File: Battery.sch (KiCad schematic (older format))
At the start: 23 parts, among them J3 USB_C_Receptacle_USB2.0, SW2 SW_SPDT, U4 SY6926

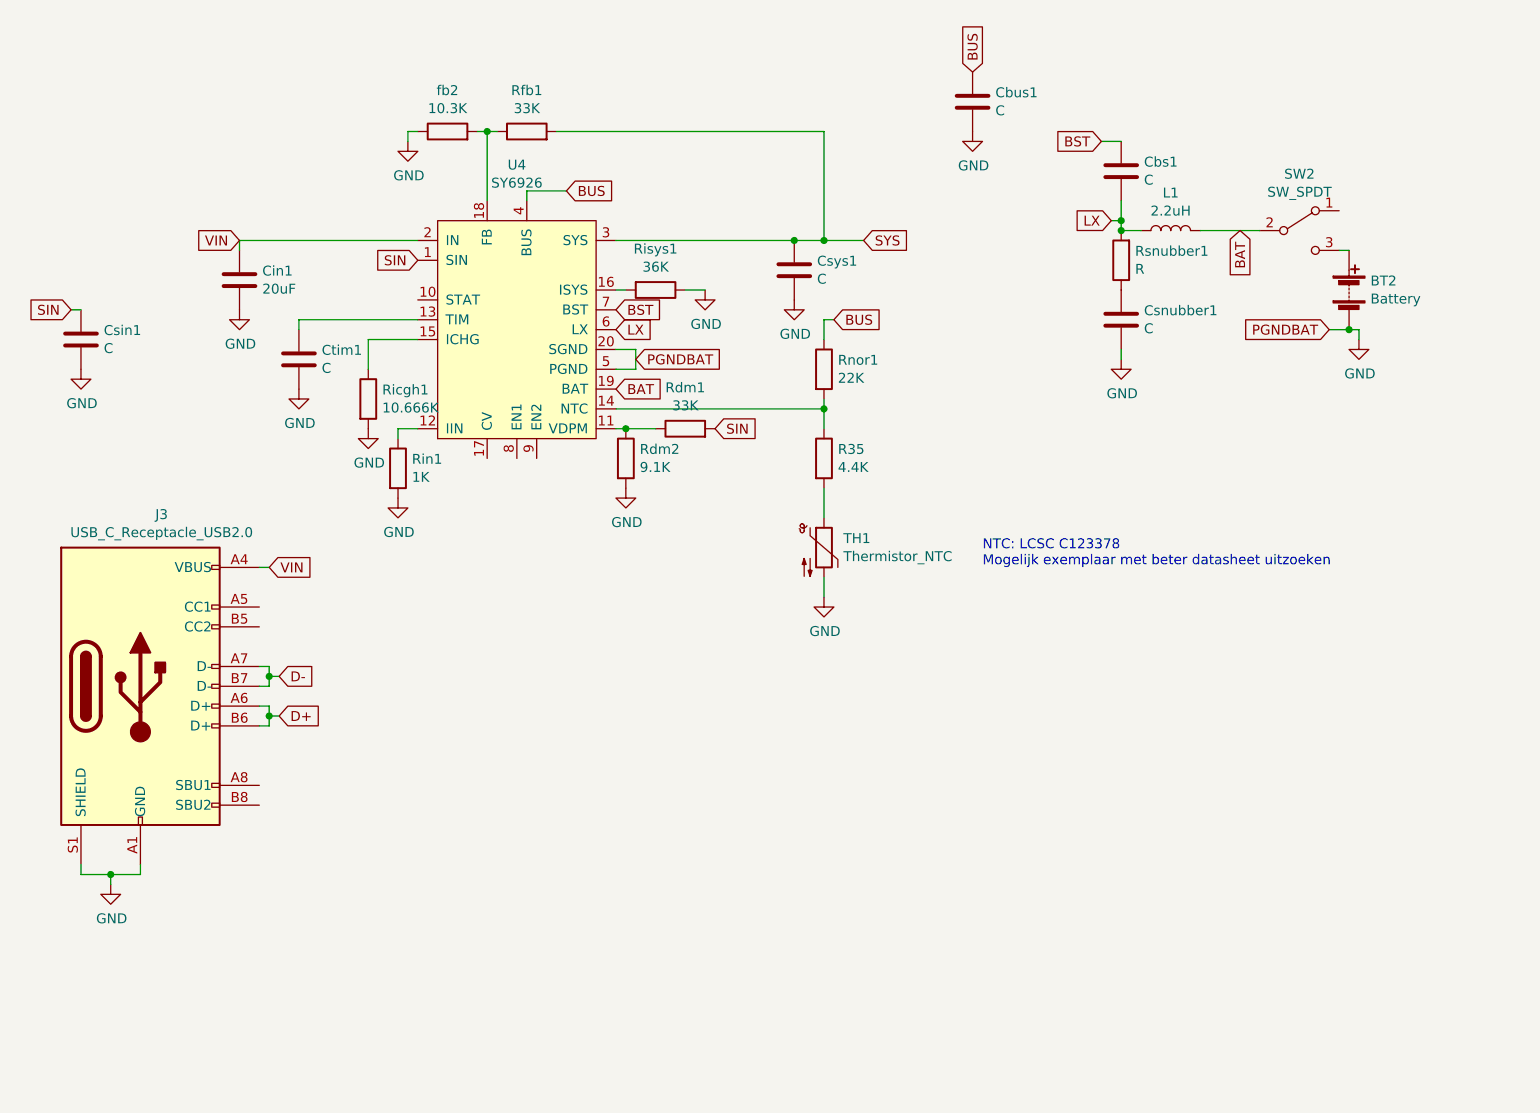
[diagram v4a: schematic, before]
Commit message: Added a rotary encoder and almost all BC values
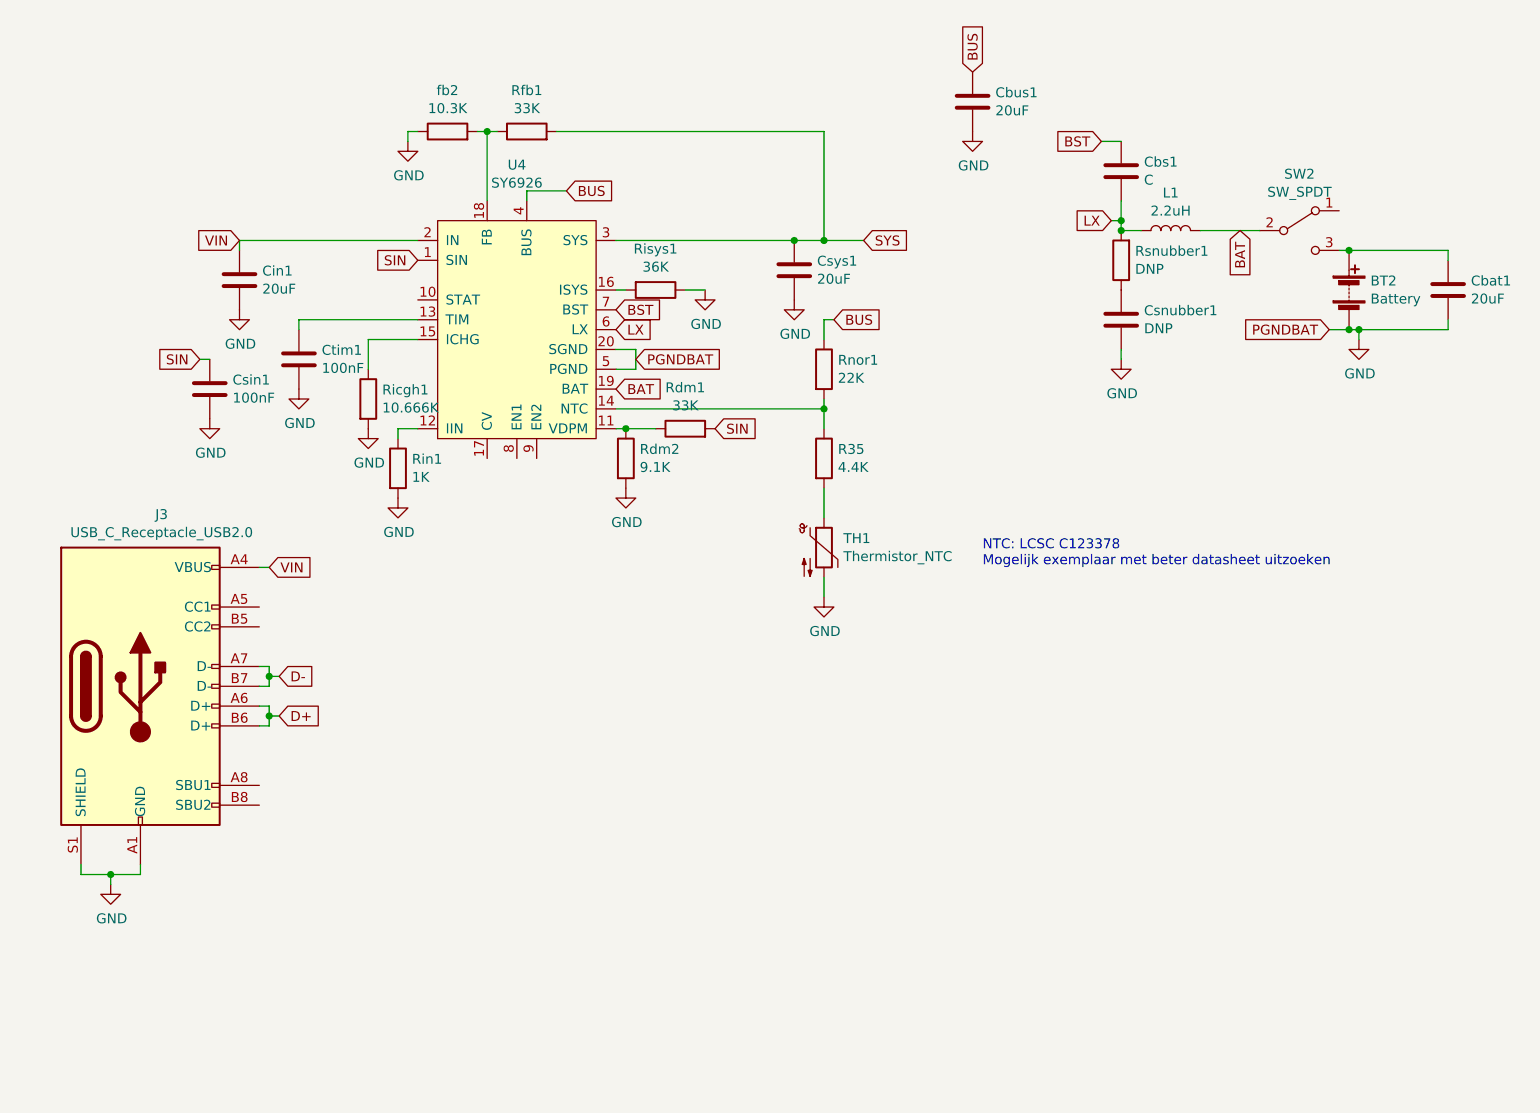
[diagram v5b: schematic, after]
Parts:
- added Cbat1: 20uF, Capacitor_SMD:C_0805_2012Metric, symbol Device:C
- Cbus1, Csys1: value C -> 20uF
- Csin1, Ctim1: value C -> 100nF
- Csnubber1: value C -> DNP
- Rsnubber1: value R -> DNP
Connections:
- net GND: now also Cbat1.2
- net at BT2.1 (+), SW2.3 (C): now also Cbat1.1
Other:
- moved on the sheet: Csin1
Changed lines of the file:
@@
-$EndComp
-$Comp
-L Device:C Cbs1
-U 1 1 60BFBF81
-P 6150 1800
-F 0 "Cbs1" H 6265 1846 50  0000 L CNN
-F 1 "C" H 6265 1755 50  0000 L CNN
-F 2 "Capacitor_SMD:C_0805_2012Metric" H 6188 1650 50  0001 C CNN
-F 3 "~" H 6150 1800 50  0001 C CNN
-	1    6150 1800
-	1    0    0    -1
 $EndComp
 $Comp
@@
 P 2000 2750
 F 0 "Ctim1" H 2115 2796 50  0000 L CNN
-F 1 "C" H 2115 2705 50  0000 L CNN
+F 1 "100nF" H 2115 2705 50  0000 L CNN
 F 2 "Capacitor_SMD:C_0805_2012Metric" H 2038 2600 50  0001 C CNN
 F 3 "~" H 2000 2750 50  0001 C CNN
@@
 L Device:C Csin1
 U 1 1 60C0200C
-P 900 2650
-F 0 "Csin1" H 1015 2696 50  0000 L CNN
-F 1 "C" H 1015 2605 50  0000 L CNN
-F 2 "Capacitor_SMD:C_0805_2012Metric" H 938 2500 50  0001 C CNN
-F 3 "~" H 900 2650 50  0001 C CNN
-	1    900  2650
+P 1550 2900
+F 0 "Csin1" H 1665 2946 50  0000 L CNN
+F 1 "100nF" H 1665 2855 50  0000 L CNN
+F 2 "Capacitor_SMD:C_0805_2012Metric" H 1588 2750 50  0001 C CNN
+F 3 "~" H 1550 2900 50  0001 C CNN
+	1    1550 2900
 	1    0    0    -1
 $EndComp
@@
 P 4500 2300
 F 0 "Csys1" H 4615 2346 50  0000 L CNN
-F 1 "C" H 4615 2255 50  0000 L CNN
+F 1 "20uF" H 4615 2255 50  0000 L CNN
 F 2 "Capacitor_SMD:C_0805_2012Metric" H 4538 2150 50  0001 C CNN
 F 3 "~" H 4500 2300 50  0001 C CNN
@@
 	6050 1650 6150 1650
 $Comp
-L Device:R Rsnubber1
-U 1 1 60C19527
-P 6150 2250
-F 0 "Rsnubber1" H 6080 2204 50  0000 R CNN
-F 1 "R" H 6080 2295 50  0000 R CNN
-F 2 "Resistor_SMD:R_0805_2012Metric" V 6080 2250 50  0001 C CNN
-F 3 "~" H 6150 2250 50  0001 C CNN
-	1    6150 2250
-	-1   0    0    1
-$EndComp
-$Comp
 L Device:C Csnubber1
 U 1 1 60C1A249
 P 6150 2550
 F 0 "Csnubber1" H 6265 2596 50  0000 L CNN
-F 1 "C" H 6265 2505 50  0000 L CNN
+F 1 "DNP" H 6265 2505 50  0000 L CNN
 F 2 "Capacitor_SMD:C_0805_2012Metric" H 6188 2400 50  0001 C CNN
 F 3 "~" H 6150 2550 50  0001 C CNN
@@
 L power:GND #PWR01
 U 1 1 60C26847
-P 900 2800
-F 0 "#PWR01" H 900 2550 50  0001 C CNN
-F 1 "GND" H 905 2627 50  0000 C CNN
-F 2 "" H 900 2800 50  0001 C CNN
-F 3 "" H 900 2800 50  0001 C CNN
-	1    900  2800
+P 1550 3050
+F 0 "#PWR01" H 1550 2800 50  0001 C CNN
+F 1 "GND" H 1555 2877 50  0000 C CNN
+F 2 "" H 1550 3050 50  0001 C CNN
+F 3 "" H 1550 3050 50  0001 C CNN
+	1    1550 3050
 	1    0    0    -1
 $EndComp
@@
 Wire Wire Line
 	2000 2550 2000 2600
-Text GLabel 850  2500 0    50   Input ~ 0
+Text GLabel 1500 2750 0    50   Input ~ 0
 SIN
 Wire Wire Line
-	850  2500 900  2500
+	1500 2750 1550 2750
 $Comp
 L Device:R fb2
@@
 P 5400 1450
 F 0 "Cbus1" H 5515 1496 50  0000 L CNN
-F 1 "C" H 5515 1405 50  0000 L CNN
+F 1 "20uF" H 5515 1405 50  0000 L CNN
 F 2 "Capacitor_SMD:C_0805_2012Metric" H 5438 1300 50  0001 C CNN
 F 3 "~" H 5400 1450 50  0001 C CNN
@@
 Wire Wire Line
 	3600 3000 4650 3000
+$Comp
+L Device:R Rsnubber1
+U 1 1 60C19527
+P 6150 2250
+F 0 "Rsnubber1" H 6080 2204 50  0000 R CNN
+F 1 "DNP" H 6080 2295 50  0000 R CNN
+F 2 "Resistor_SMD:R_0805_2012Metric" V 6080 2250 50  0001 C CNN
+F 3 "~" H 6150 2250 50  0001 C CNN
+	1    6150 2250
+	-1   0    0    1
+$EndComp
+$Comp
+L Device:C Cbs1
+U 1 1 60BFBF81
+P 6150 1800
+F 0 "Cbs1" H 6265 1846 50  0000 L CNN
+F 1 "C" H 6265 1755 50  0000 L CNN
+F 2 "Capacitor_SMD:C_0805_2012Metric" H 6188 1650 50  0001 C CNN
+F 3 "~" H 6150 1800 50  0001 C CNN
+	1    6150 1800
+	1    0    0    -1
+$EndComp
+$Comp
+L Device:C Cbat1
+U 1 1 60D9E5BD
+P 7800 2400
+F 0 "Cbat1" H 7915 2446 50  0000 L CNN
+F 1 "20uF" H 7915 2355 50  0000 L CNN
+F 2 "Capacitor_SMD:C_0805_2012Metric" H 7838 2250 50  0001 C CNN
+F 3 "~" H 7800 2400 50  0001 C CNN
+	1    7800 2400
+	1    0    0    -1
+$EndComp
+Wire Wire Line
+	7300 2200 7800 2200
+Wire Wire Line
+	7800 2200 7800 2250
+Connection ~ 7300 2200
+Wire Wire Line
+	7800 2550 7800 2600
+Wire Wire Line
+	7800 2600 7350 2600
+Connection ~ 7350 2600
 $EndSCHEMATC

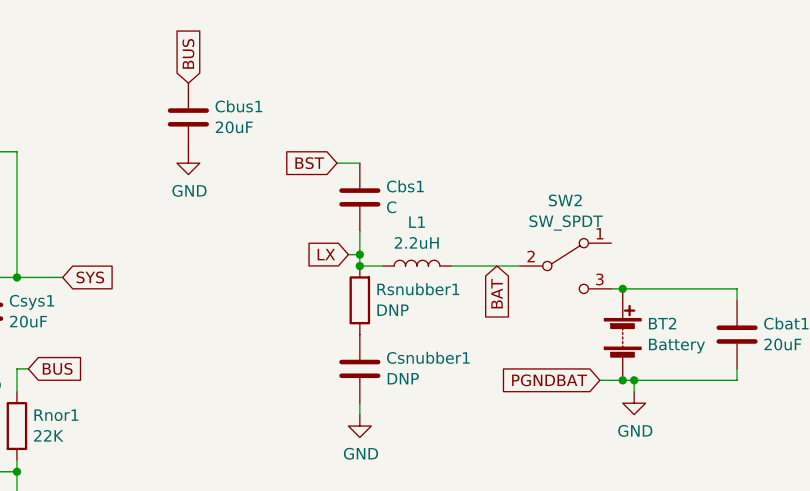
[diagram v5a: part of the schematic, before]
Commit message: Final schematic edits, PCB layout
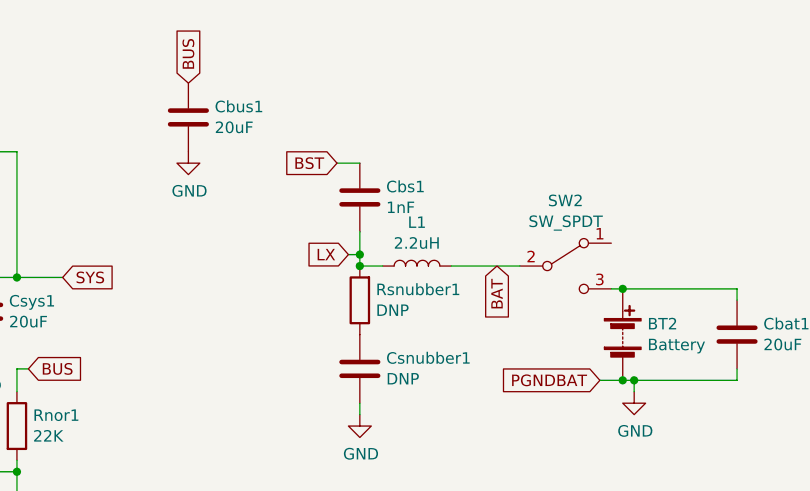
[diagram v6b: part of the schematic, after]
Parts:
- Cbs1: value C -> 1nF
- L1: footprint Connector_PinHeader_2.54mm:PinHeader_1x02_P2.54mm_Vertical -> Inductor_SMD:L_Sunlord_MWSA0518_5.4x5.2mm
- R35: footprint (none) -> Resistor_SMD:R_0805_2012Metric
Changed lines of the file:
@@
 $Descr A4 11693 8268
 encoding utf-8
-Sheet 3 5
+Sheet 3 6
 Title "Battery"
 Date ""
@@
 F 0 "L1" V 6590 2100 50  0000 C CNN
 F 1 "2.2uH" V 6499 2100 50  0000 C CNN
-F 2 "Connector_PinHeader_2.54mm:PinHeader_1x02_P2.54mm_Vertical" H 6400 2100 50  0001 C CNN
+F 2 "Inductor_SMD:L_Sunlord_MWSA0518_5.4x5.2mm" H 6400 2100 50  0001 C CNN
 F 3 "~" H 6400 2100 50  0001 C CNN
 	1    6400 2100
@@
 F 0 "R35" H 4720 3296 50  0000 L CNN
 F 1 "4.4K" H 4720 3205 50  0000 L CNN
-F 2 "" V 4580 3250 50  0001 C CNN
+F 2 "Resistor_SMD:R_0805_2012Metric" V 4580 3250 50  0001 C CNN
 F 3 "~" H 4650 3250 50  0001 C CNN
 	1    4650 3250
@@
 P 6150 1800
 F 0 "Cbs1" H 6265 1846 50  0000 L CNN
-F 1 "C" H 6265 1755 50  0000 L CNN
+F 1 "1nF" H 6265 1755 50  0000 L CNN
 F 2 "Capacitor_SMD:C_0805_2012Metric" H 6188 1650 50  0001 C CNN
 F 3 "~" H 6150 1800 50  0001 C CNN

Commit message: pretty much routed everything
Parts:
- renumbered BT2 to BT1
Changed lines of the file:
@@
 $EndComp
 $Comp
-L Device:Battery BT2
+L Device:Battery BT1
 U 1 1 60BFF57C
 P 7300 2400
-F 0 "BT2" H 7408 2446 50  0000 L CNN
+F 0 "BT1" H 7408 2446 50  0000 L CNN
 F 1 "Battery" H 7408 2355 50  0000 L CNN
 F 2 "Connector_PinHeader_2.54mm:PinHeader_1x02_P2.54mm_Vertical" V 7300 2460 50  0001 C CNN

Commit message: Fixed some DRC errors and some incorrect wiring
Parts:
- TH1: footprint (none) -> Connector_PinHeader_2.54mm:PinHeader_1x02_P2.54mm_Vertical
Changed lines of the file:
@@
 F 0 "TH1" H 4748 3746 50  0000 L CNN
 F 1 "Thermistor_NTC" H 4748 3655 50  0000 L CNN
-F 2 "" H 4650 3750 50  0001 C CNN
+F 2 "Connector_PinHeader_2.54mm:PinHeader_1x02_P2.54mm_Vertical" H 4650 3750 50  0001 C CNN
 F 3 "~" H 4650 3750 50  0001 C CNN
 	1    4650 3700
